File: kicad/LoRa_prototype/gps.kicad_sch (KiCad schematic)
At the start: 25 parts, among them J10 I2C_BME, J11 BME, J12 GPS, J13 GPS_UART, J8 BMV, J9 I2C_BMV, Q1 DTC143Z, Q2 DTC143Z, U6 L80-R, U7 BME688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

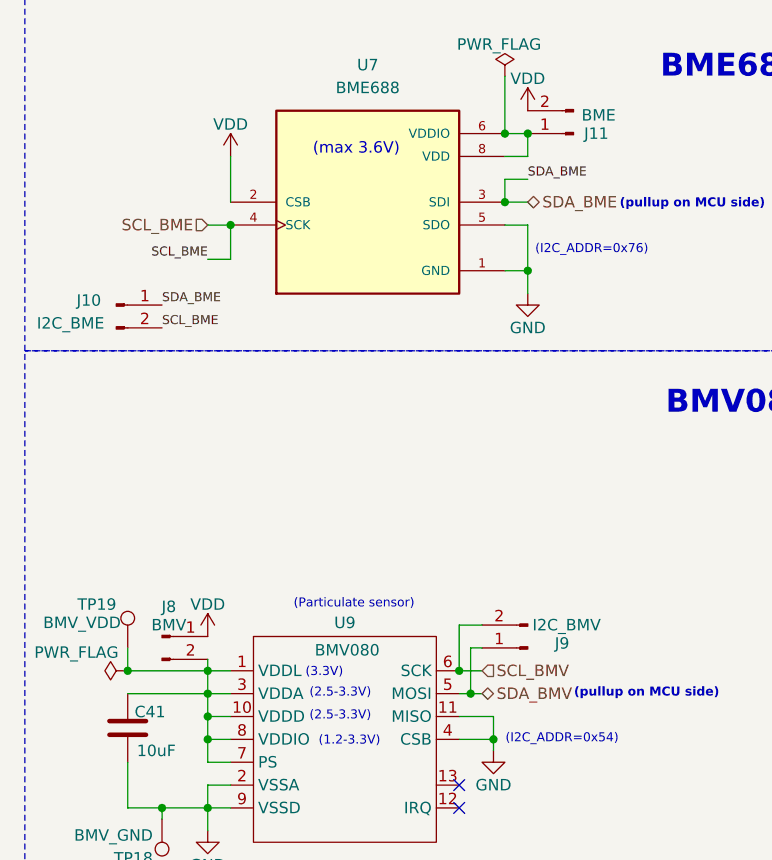
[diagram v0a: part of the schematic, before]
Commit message: Removed redundant I2C test pin headers
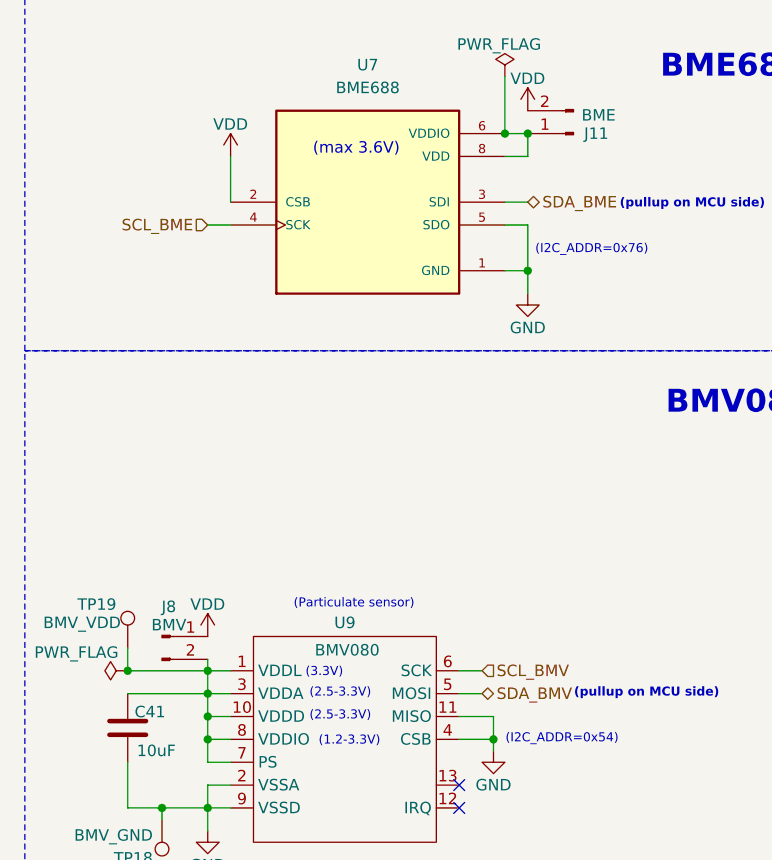
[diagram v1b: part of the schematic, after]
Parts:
- removed J10: I2C_BME, Connector_PinHeader_2.54mm:PinHeader_1x02_P2.54mm_Vertical, symbol Connector:Conn_01x02_Pin
- removed J9: I2C_BMV, Connector_PinHeader_2.54mm:PinHeader_1x02_P2.54mm_Vertical, symbol Connector:Conn_01x02_Pin

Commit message: Assigned most footprints
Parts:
- TP15, TP16, TP17, TP18, TP19: footprint (none) -> TestPoint:TestPoint_Pad_2.0x2.0mm
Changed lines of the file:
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@@
 			)
 		)
-		(property "Footprint" ""
+		(property "Footprint" "TestPoint:TestPoint_Pad_2.0x2.0mm"
 			(at 194.31 86.36 0)
 			(hide yes)
@@
 			)
 		)
-		(property "Footprint" ""
+		(property "Footprint" "TestPoint:TestPoint_Pad_2.0x2.0mm"
 			(at 237.49 93.98 0)
 			(hide yes)
@@
 			)
 		)
-		(property "Footprint" ""
+		(property "Footprint" "TestPoint:TestPoint_Pad_2.0x2.0mm"
 			(at 196.85 124.46 0)
 			(hide yes)
@@
 			)
 		)
-		(property "Footprint" ""
+		(property "Footprint" "TestPoint:TestPoint_Pad_2.0x2.0mm"
 			(at 35.56 149.86 0)
 			(hide yes)
@@
 			)
 		)
-		(property "Footprint" ""
+		(property "Footprint" "TestPoint:TestPoint_Pad_2.0x2.0mm"
 			(at 41.91 130.81 0)
 			(hide yes)

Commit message: Started PCB Layout (Milestone)
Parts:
- U7: footprint BME688:IC_BME688 -> footprints:IC_BME688
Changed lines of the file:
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@@
 			)
 		)
-		(property "Footprint" "BME688:IC_BME688"
+		(property "Footprint" "footprints:IC_BME688"
 			(at 63.5 81.28 0)
 			(hide yes)

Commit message: Stable commit
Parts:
- removed J13: GPS_UART, Connector_PinHeader_2.54mm:PinHeader_1x02_P2.54mm_Vertical, symbol Connector:Conn_01x02_Pin
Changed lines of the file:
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@@
 	)
 	(junction
-		(at 243.84 97.79)
-		(diameter 0)
-		(color 0 0 0 0)
-	)
-	(junction
 		(at 77.47 140.97)
 		(diameter 0)
@@
 	)
 	(junction
-		(at 243.84 107.95)
-		(diameter 0)
-		(color 0 0 0 0)
-	)
-	(junction
 		(at 45.72 138.43)
 		(diameter 0)
@@
 	(wire
 		(pts
-			(xy 243.84 107.95) (xy 245.11 107.95)
+			(xy 242.57 107.95) (xy 245.11 107.95)
 		)
 		(stroke
@@
 	(wire
 		(pts
-			(xy 243.84 104.14) (xy 243.84 107.95)
-		)
-		(stroke
-			(width 0)
-			(type default)
-		)
-	)
-	(wire
-		(pts
 			(xy 36.83 133.35) (xy 45.72 133.35)
 		)
@@
 	(wire
 		(pts
-			(xy 242.57 107.95) (xy 243.84 107.95)
-		)
-		(stroke
-			(width 0)
-			(type default)
-		)
-	)
-	(wire
-		(pts
-			(xy 243.84 101.6) (xy 243.84 97.79)
-		)
-		(stroke
-			(width 0)
-			(type default)
-		)
-	)
-	(wire
-		(pts
 			(xy 81.28 88.9) (xy 81.28 91.44)
 		)
@@
 	(wire
 		(pts
-			(xy 243.84 97.79) (xy 242.57 97.79)
-		)
-		(stroke
-			(width 0)
-			(type default)
-		)
-	)
-	(wire
-		(pts
-			(xy 245.11 101.6) (xy 243.84 101.6)
-		)
-		(stroke
-			(width 0)
-			(type default)
-		)
-	)
-	(wire
-		(pts
 			(xy 45.72 143.51) (xy 45.72 140.97)
 		)
@@
 	(wire
 		(pts
-			(xy 245.11 97.79) (xy 243.84 97.79)
+			(xy 242.57 97.79) (xy 245.11 97.79)
 		)
 		(stroke
@@
 	(wire
 		(pts
-			(xy 245.11 104.14) (xy 243.84 104.14)
-		)
-		(stroke
-			(width 0)
-			(type default)
-		)
-	)
-	(wire
-		(pts
 			(xy 36.83 135.89) (xy 45.72 135.89)
 		)
@@
 	)
 	(symbol
-		(lib_id "Connector:Conn_01x02_Pin")
-		(at 250.19 104.14 180)
-		(unit 1)
-		(body_style 1)
-		(exclude_from_sim no)
-		(in_bom yes)
-		(on_board yes)
-		(in_pos_files yes)
-		(dnp no)
-		(property "Reference" "J13"
-			(at 252.222 103.632 0)
-			(hide yes)
-			(show_name no)
-			(do_not_autoplace no)
-			(effects
-				(font
-					(size 1.27 1.27)
-				)
-			)
-		)
-		(property "Value" "GPS_UART"
-			(at 252.73 102.87 0)
-			(show_name no)
-			(do_not_autoplace no)
-			(effects
-				(font
-					(size 1.27 1.27)
-				)
-			)
-		)
-		(property "Footprint" "Connector_PinHeader_2.54mm:PinHeader_1x02_P2.54mm_Vertical"
-			(at 250.19 104.14 0)
-			(hide yes)
-			(show_name no)
-			(do_not_autoplace no)
-			(effects
-				(font
-					(size 1.27 1.27)
-				)
-			)
-		)
-		(property "Datasheet" ""
-			(at 250.19 104.14 0)
-			(hide yes)
-			(show_name no)
-			(do_not_autoplace no)
-			(effects
-				(font
-					(size 1.27 1.27)
-				)
-			)
-		)
-		(property "Description" "Generic connector, single row, 01x02, script generated"
-			(at 250.19 104.14 0)
-			(hide yes)
-			(show_name no)
-			(do_not_autoplace no)
-			(effects
-				(font
-					(size 1.27 1.27)
-				)
-			)
-		)
-		(pin "1"
-		)
-		(pin "2"
-		)
-		(instances
-			(project "LoRa_prototype"
-				(path "/9fad4700-f514-47ad-821a-b4076ecc08de/0b8e018d-1945-475c-8020-0cbd093bbf1b"
-					(reference "J13")
-					(unit 1)
-				)
-			)
-		)
-	)
-	(symbol
 		(lib_id "Device:C")
 		(at 215.9 90.17 0)
@@
 			"2c35bedd-fcbf-4d32-9b4e-ed4e5da841c8" "2c38807a-03e7-441b-a256-9e72f65b939f"
 			"2fabffcb-c1d2-41cd-b183-87d9a1992ee9" "3451803d-e6d9-4acc-9003-5d16643f7c75"
-			"3f5b329a-107b-4462-8278-4257294720df" "40e90838-ed06-4898-8daa-a3bb260bff82"
-			"426a0f97-bc73-4bf4-9784-86589b59a417" "4623f308-ea1c-4203-b8dc-3f4a4c255c84"
-			"513147d1-f11a-453b-80ee-ea26f416ad26" "517842e3-f092-4cfa-8895-b688807d1845"
-			"51a3c71a-2247-4cec-977b-f8484733df25" "530a012b-6fc2-402a-9cb2-c1f095dc7608"
-			"541d1692-6320-4c6e-ae96-d899dc2031a3" "55d45147-62da-40ef-858b-5a164cefdcdc"
-			"58c61b03-6afe-47c7-bcaa-f476ddbfa2d7" "5c089622-4136-4729-bf03-e2b3d92aecc3"
-			"5f238252-9f3e-4fb8-83e0-fe63b412dc79" "6146a8ba-d5a4-4bd4-bea5-f070c9e4481f"
-			"61fb6ae8-c1d6-4718-a2c8-f9f3cd78b6b5" "630e9ec7-6581-475d-9246-98420c2d391c"
-			"6c9aac45-7e46-4ff4-aa33-70bb34ea0ccf" "6fd954bc-a86f-4d13-b0fc-55238a90606c"
-			"701515e0-b205-432f-9371-cdd56e7e5cc9" "751c4c11-1c55-4068-b5cb-9faea4731d3d"
+			"40e90838-ed06-4898-8daa-a3bb260bff82" "426a0f97-bc73-4bf4-9784-86589b59a417"
+			"4623f308-ea1c-4203-b8dc-3f4a4c255c84" "513147d1-f11a-453b-80ee-ea26f416ad26"
+			"517842e3-f092-4cfa-8895-b688807d1845" "51a3c71a-2247-4cec-977b-f8484733df25"
+			"530a012b-6fc2-402a-9cb2-c1f095dc7608" "541d1692-6320-4c6e-ae96-d899dc2031a3"
+			"55d45147-62da-40ef-858b-5a164cefdcdc" "58c61b03-6afe-47c7-bcaa-f476ddbfa2d7"
+			"5c089622-4136-4729-bf03-e2b3d92aecc3" "5f238252-9f3e-4fb8-83e0-fe63b412dc79"
+			"6146a8ba-d5a4-4bd4-bea5-f070c9e4481f" "61fb6ae8-c1d6-4718-a2c8-f9f3cd78b6b5"
+			"630e9ec7-6581-475d-9246-98420c2d391c" "6c9aac45-7e46-4ff4-aa33-70bb34ea0ccf"
+			"6fd954bc-a86f-4d13-b0fc-55238a90606c" "701515e0-b205-432f-9371-cdd56e7e5cc9"
 			"75226741-1611-4248-ac28-36d4b81fc71a" "77f45b81-4e9e-40b9-b524-0c9b3f9fc006"
 			"7cb88c24-4af9-4781-98b6-f9e708618d58" "8049ae7e-f2a6-45a8-90b0-668874b4cf3f"
 			"86062615-63b8-4de3-92c4-12fdf3da5f0f" "8944d50c-d4c9-4c9f-b2e9-17d1fe0dcc33"
-			"8a64d92b-301f-4b68-9be7-8502a3830d17" "8c3d92c9-1132-48c6-b8b7-599e8e685a4e"
-			"8d4f34ca-e747-42ca-8b79-386164827d5e" "911aef47-ba59-473f-98d0-07498cc7828b"
-			"93484f41-8d50-4221-bbc7-78895ecd7cb5" "958f7af2-6b11-4244-8961-dc3cc262d293"
-			"99732437-9e5a-423a-9214-78f67400d73b" "9a889956-70e4-432a-91c9-5c5866fc54aa"
-			"9bc52e8d-6496-4eec-bfe7-d9974090dcbb" "9da5000e-2b3c-486a-9db0-2fdf2e62ea1a"
+			"8c3d92c9-1132-48c6-b8b7-599e8e685a4e" "8d4f34ca-e747-42ca-8b79-386164827d5e"
+			"911aef47-ba59-473f-98d0-07498cc7828b" "93484f41-8d50-4221-bbc7-78895ecd7cb5"
+			"958f7af2-6b11-4244-8961-dc3cc262d293" "99732437-9e5a-423a-9214-78f67400d73b"
+			"9a889956-70e4-432a-91c9-5c5866fc54aa" "9da5000e-2b3c-486a-9db0-2fdf2e62ea1a"
 			"9e70c82b-7979-4ac3-a926-fc9869dd63e1" "b16ee325-5169-44d5-842c-aba7c451a76a"
 			"c2247284-81ca-40a9-9abd-0d6389a79385" "c3ff54d6-b1d2-4d93-92b7-f5a3d73e0f63"
 			"c568cd9b-3468-4ebc-8d7e-da10856e38f8" "c62084ce-50ac-48d6-846d-2f3cae359cf8"
-			"c698f745-6df9-4774-b4ca-f5f00de3171a" "c8846517-8f6a-4ddb-bc4c-dd7e0fd02364"
-			"ca8b0004-50ed-40bd-8c3f-db95ce2e0a5a" "cdba45bd-3f2d-45da-9443-9d8f5bce30f9"
+			"c698f745-6df9-4774-b4ca-f5f00de3171a" "cdba45bd-3f2d-45da-9443-9d8f5bce30f9"
 			"d0527ade-5d30-4974-a7da-e6aeb1270672" "d546c965-833c-48e8-98c4-cce19943692e"
 			"d6d5a5e4-698c-4ba8-b3a6-e613dc3648f5" "d712f0c2-18ab-495c-837b-f3930f427e6f"
-			"d84f4587-72fb-483e-98b7-0990ed2c7482" "dc4b760d-4842-43d9-ada5-52d0ab50fe01"
 			"dece62fd-28c3-4458-97cf-cc1e82e93997" "e7dcbc73-077e-4ab6-a854-ee5095615ce5"
 			"e970cc6c-0aee-4898-870d-227a23d4ba6a" "f0b9fc72-b85b-4b66-aece-5923a7d9e319"
 			"f4a63cd3-e266-4237-ab58-7597ac4aac55" "f640938c-93ae-47af-8e19-dfeea7133d1e"
-			"f97b8290-151e-4a00-b753-b38f407e1d3f" "fcf570ba-5abf-4e03-b7f2-2e0382e257ba"
-			"fe22b8a6-108d-4c06-93c4-1abc8e4bd102" "ff5b4799-cc73-408d-a75d-743d984c5c24"
+			"fcf570ba-5abf-4e03-b7f2-2e0382e257ba" "fe22b8a6-108d-4c06-93c4-1abc8e4bd102"
+			"ff5b4799-cc73-408d-a75d-743d984c5c24"
 		)
 	)

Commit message: Changed decoupling in schematic
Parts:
- C38, C40, C41: footprint Capacitor_SMD:C_0805_2012Metric -> Capacitor_SMD:C_0603_1608Metric
- C39: footprint Capacitor_SMD:C_0805_2012Metric -> Capacitor_SMD:C_0402_1005Metric
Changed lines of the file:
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@@
 			)
 		)
-		(property "Footprint" "Capacitor_SMD:C_0805_2012Metric"
+		(property "Footprint" "Capacitor_SMD:C_0402_1005Metric"
 			(at 199.0852 93.98 0)
 			(hide yes)
@@
 			)
 		)
-		(property "Footprint" "Capacitor_SMD:C_0805_2012Metric"
+		(property "Footprint" "Capacitor_SMD:C_0603_1608Metric"
 			(at 216.8652 93.98 0)
 			(hide yes)
@@
 			)
 		)
-		(property "Footprint" "Capacitor_SMD:C_0805_2012Metric"
+		(property "Footprint" "Capacitor_SMD:C_0603_1608Metric"
 			(at 190.1952 93.98 0)
 			(hide yes)
@@
 			)
 		)
-		(property "Footprint" "Capacitor_SMD:C_0805_2012Metric"
+		(property "Footprint" "Capacitor_SMD:C_0603_1608Metric"
 			(at 37.7952 143.51 0)
 			(hide yes)

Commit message: Stable commit (22 DRC warnings only)
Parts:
- U9: LCSC (none) -> C587979
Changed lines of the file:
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@@
+			)
+		)
+		(property "LCSC" "C587979"
+			(at 60.96 139.7 0)
+			(hide yes)
+			(show_name no)
+			(do_not_autoplace no)
+			(effects
+				(font
+					(size 1.27 1.27)
+				)
 			)
 		)

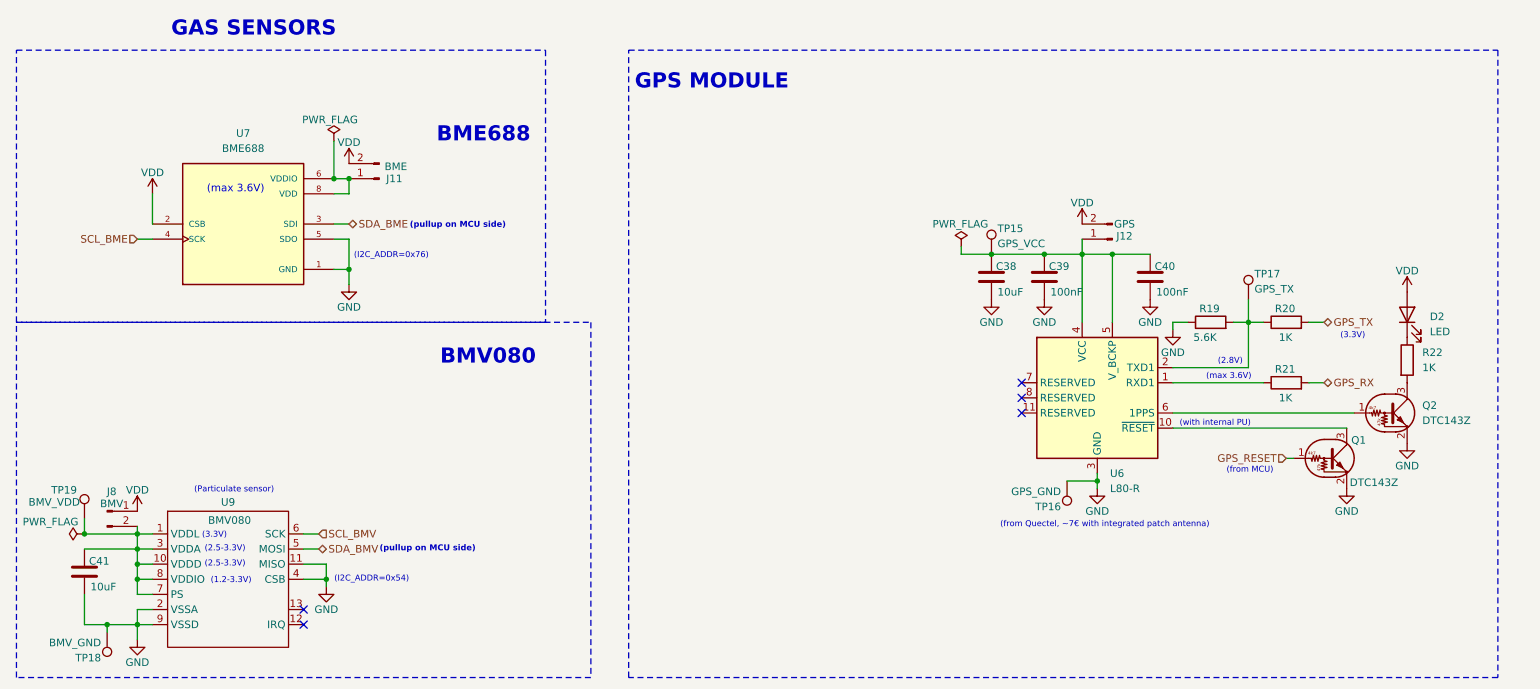
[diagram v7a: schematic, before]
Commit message: Replaced DTC143ZEBTL with basic parts
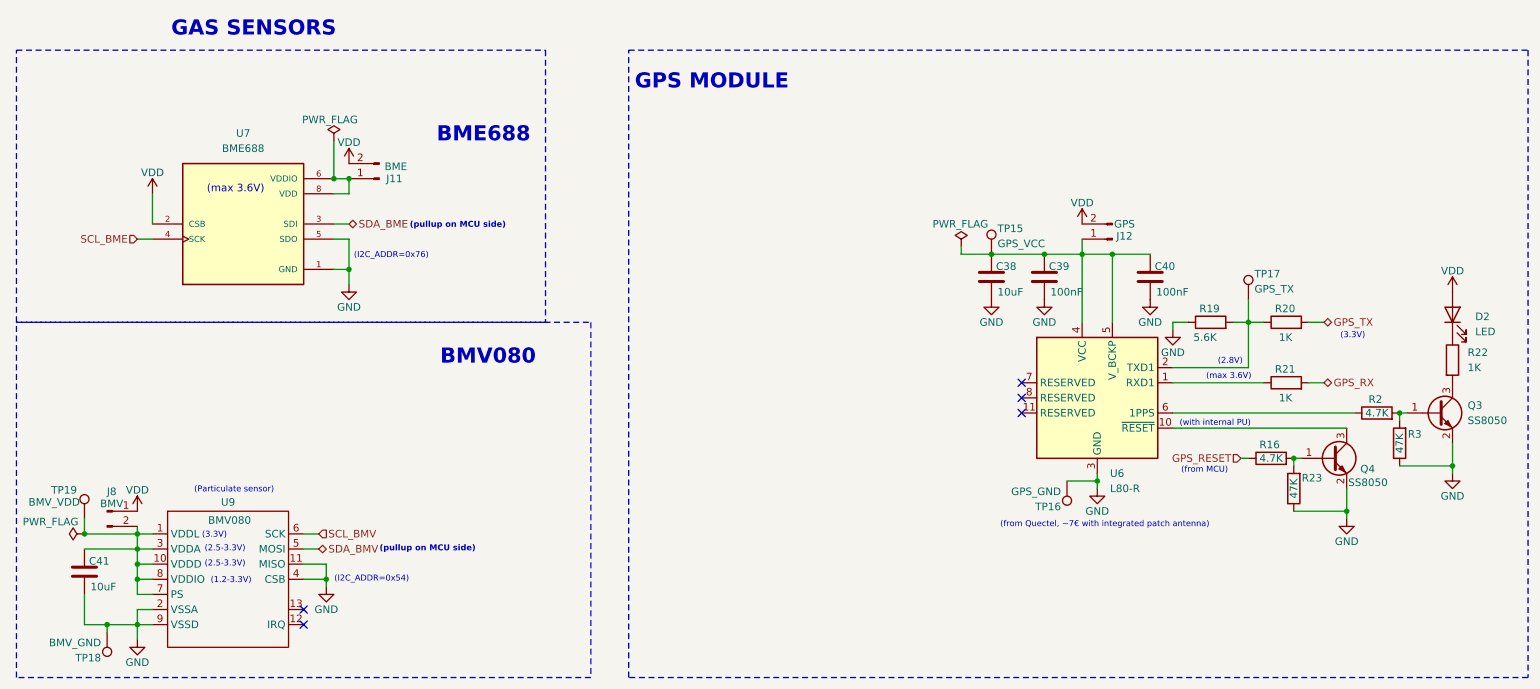
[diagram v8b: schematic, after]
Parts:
- removed Q1, Q2: DTC143Z, footprints:SOTFL50P160X85-3N, symbol Transistor_BJT:DTC143Z
- added Q3, Q4: SS8050, Package_TO_SOT_SMD:SOT-23, symbol Transistor_BJT:SS8050
- added R16, R2: 4.7K, Resistor_SMD:R_0805_2012Metric, symbol Device:R
- added R23, R3: 47K, Resistor_SMD:R_0805_2012Metric, symbol Device:R
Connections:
- net GND: now also Q3.2 (E), Q4.2 (E), R23.1, R3.1
- net GPS_RESET: now also R16.1
- net at U6.10 (~{RESET}): now also Q4.3 (C)
- net at U6.6 (1PPS): now also R2.1
- net at R22.2: now also Q3.3 (C)
- new net: Q4.1 (B), R16.2, R23.2
- new net: Q3.1 (B), R2.2, R3.2
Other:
- moved on the sheet: D2, R22
